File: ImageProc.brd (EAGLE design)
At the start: 49.8 x 23.2 mm, 119 parts, among them IC1 XC61GC3002HR-G, IC10 AT45DB642D-CNU, IC2 MIC5335-SPYMT, IC3 MIC5335-JGYMT, IC4 DSPIC33FJ128MC706A, IC5 AT86RF233-ZU, IC6 LTC6088, IC7 DRV8833RTY, IC8 DRV8833RTY, IC9 MPU-6000, P1 BAT+, P10 MD2, P11 EXT1, P12 EXT2, P13 EXT3, P14 EXT4, P16 EXT5, P2 BAT-, P3 MA1, P4 MA2, P5 MB1, P6 MB2, P7 MC1, P8 MC2, P9 MD1

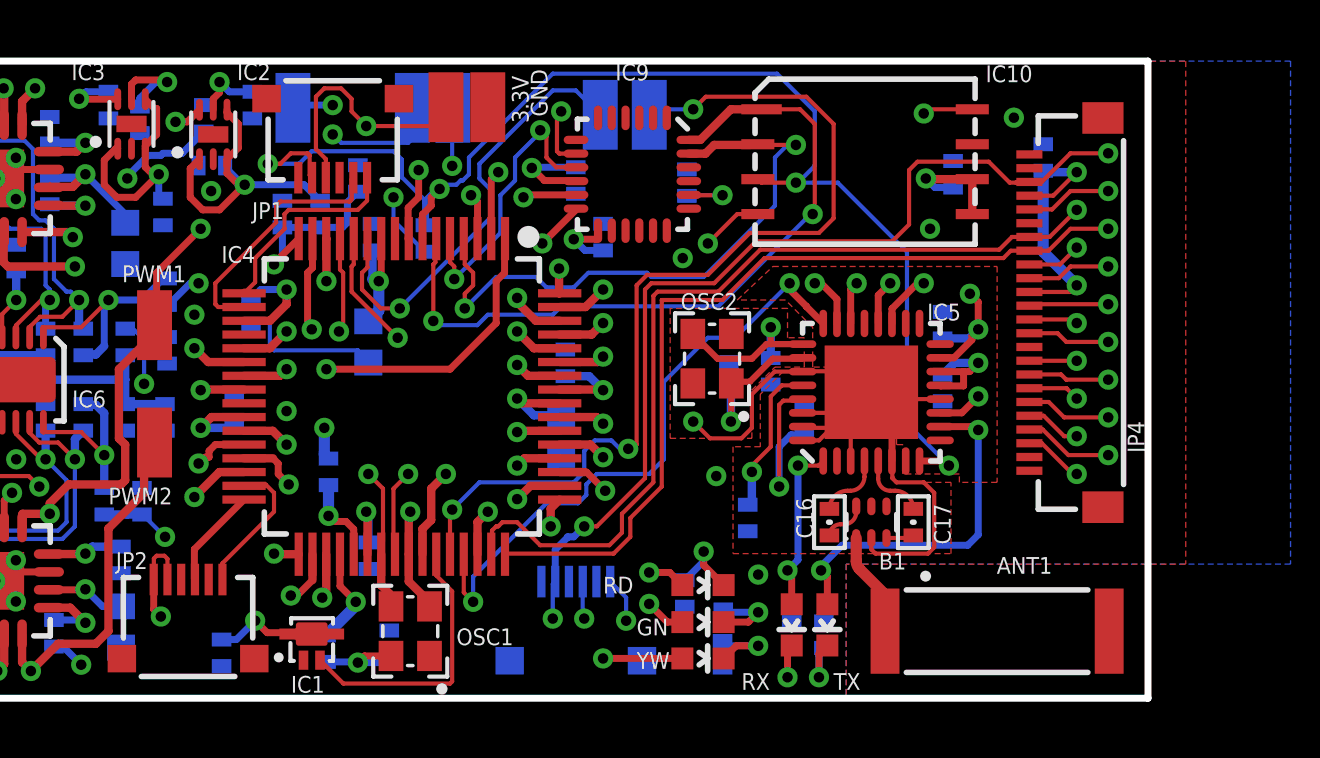
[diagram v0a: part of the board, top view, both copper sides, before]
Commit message: Initial strip of the IP2.5 Rev C board. dsPic and camera connector removed.
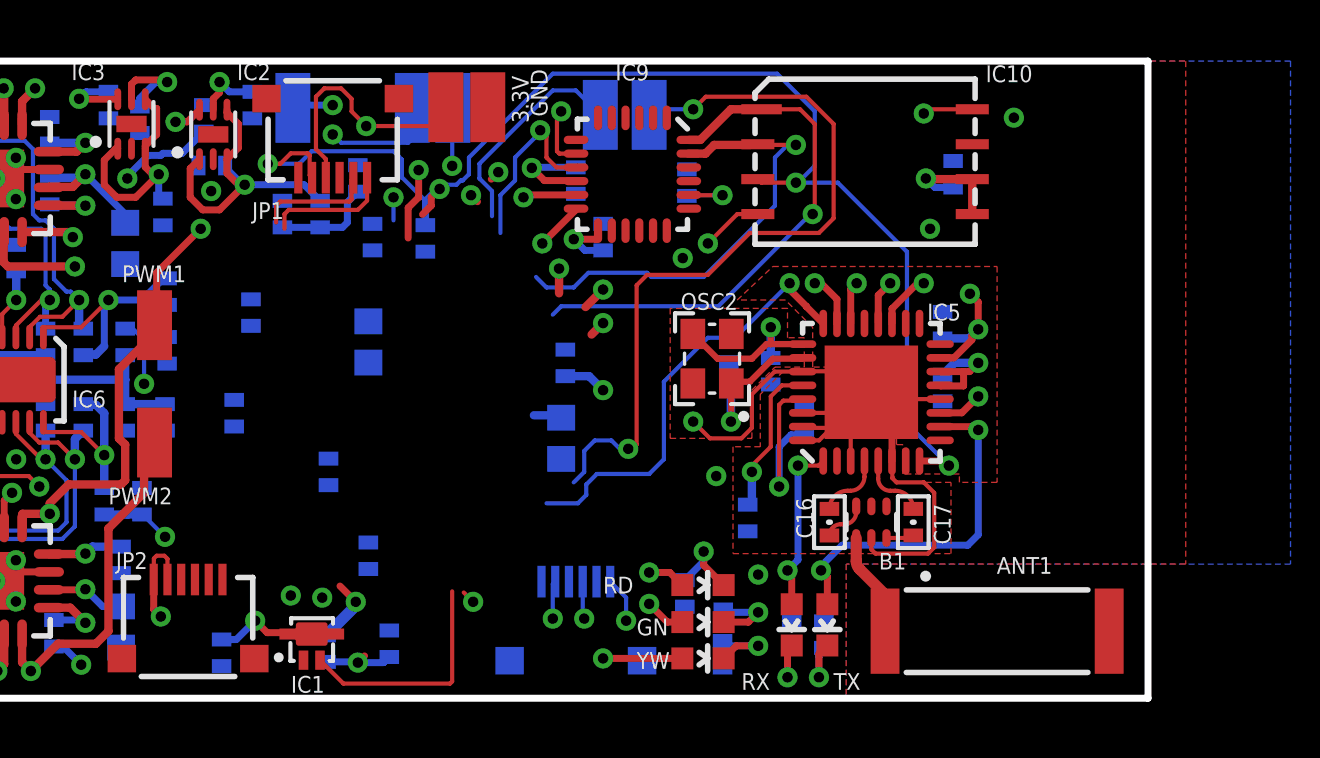
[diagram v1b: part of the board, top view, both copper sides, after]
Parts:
- removed C36: 0.1uF, biomimetic:0402-CAP
- removed IC4: DSPIC33FJ128MC706A, biomimetic:TQFP-64
- removed JP4: 51441-2493-C, biomimetic:MOLEX_52740-2490
- removed OSC1: ECS-2033-400, biomimetic:OSCILLATOR-SMD
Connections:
- removed net 40MHZ: IC4.39, JP4.12, OSC1.3
- removed net CAM_D0: IC4.46, JP4.6
- removed net CAM_D1: IC4.49, JP4.4
- removed net CAM_D2: IC4.50, JP4.3
- removed net CAM_D3: IC4.51, JP4.5
- removed net CAM_D4: IC4.52, JP4.7
- removed net CAM_D5: IC4.53, JP4.9
- removed net CAM_D6: IC4.54, JP4.11
- removed net CAM_D7: IC4.55, JP4.13
- removed net CAM_PCLK: IC4.59, JP4.8
- removed net CAM_PWDN: IC4.48, JP4.17
- removed net CAM_VSYNC: IC4.47, JP4.18
- net !RESET: no longer IC4.7
- net !SS1: no longer IC4.14
- net !SS2_1: no longer IC4.8
- net !SS2_2: no longer IC4.40
- net 1.8V: no longer JP4.15
- net 2.5V: no longer C36.2, JP4.14, JP4.21
- net 3.3V: no longer IC4.10, IC4.26, IC4.38, IC4.57, OSC1.4
- net AN1/RB1: no longer IC4.15
- net AN3/INDX/RB3: no longer IC4.13
- net AN4/QEA/IC7/RB4: no longer IC4.12
- net AN5/QEB/IC8/RB5: no longer IC4.11
- net BATT_LEVEL: no longer IC4.16
- net CAM_HREF: no longer IC4.58, JP4.16
- net GND: no longer C36.1, IC4.20, IC4.25, IC4.41, IC4.9, JP4.10, JP4.19, JP4.23, OSC1.2
- net GN_LED: no longer IC4.28
- net IC3/INT3/RD10: no longer IC4.44
- net IMU_IRQ: no longer IC4.42
- net LOWBATT_IRQ: no longer IC4.43
- net MOTOR_A_BEMF: no longer IC4.21
- net MOTOR_A_IN1: no longer IC4.61
- net MOTOR_A_IN2: no longer IC4.60
- net MOTOR_B_BEMF: no longer IC4.22
- net MOTOR_B_IN1: no longer IC4.63
- net MOTOR_B_IN2: no longer IC4.62
- net MOTOR_C_BEMF: no longer IC4.23
- net MOTOR_C_IN1: no longer IC4.1
- net MOTOR_C_IN2: no longer IC4.64
- net MOTOR_D_BEMF: no longer IC4.24
- net MOTOR_D_IN1: no longer IC4.3
- net MOTOR_D_IN2: no longer IC4.2
- net N$21: no longer IC4.19
- net N$28: no longer IC4.56
- net PGC: no longer IC4.17
- net PGD: no longer IC4.18
- net RADIO_IRQ: no longer IC4.45
- net RADIO_SLP_TR: no longer IC4.30
- net RD_LED: no longer IC4.27
- net SCK1: no longer IC4.35
- net SCK2: no longer IC4.4
- net SCL1: no longer IC4.37, JP4.20
- net SDA1: no longer IC4.36, JP4.22
- net SDI1: no longer IC4.34
- net SDI2: no longer IC4.5
- net SDO1: no longer IC4.33
- net SDO2: no longer IC4.6
- net U2RX: no longer IC4.31
- net U2TX: no longer IC4.32
- net YW_LED: no longer IC4.29
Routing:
- net SCL1: track 56.4 -> 1.37 mm, vias 3 -> 1
- net 2.5V: track 51.9 -> 2.59 mm, vias 3 -> 1
- net MOTOR_A_IN1: track 50.6 -> 1.92 mm
- net 1.8V: track 48.3 -> 3.48 mm, vias 2 -> 1
- net MOTOR_A_IN2: track 45.6 -> 1.77 mm, vias 3 -> 2
- net SDA1: track 45.6 -> 3.86 mm, vias 4 -> 2
- net RADIO_SLP_TR: track 41.3 -> 1.63 mm, vias 2 -> 1
- net 40MHZ: track 38.6 -> 0.00 mm, vias 2 -> 0
- net CAM_HREF: track 35.7 -> 1.95 mm, vias 3 -> 1
- net MOTOR_C_IN1: track 34.5 -> 1.37 mm, vias 2 -> 1
- net MOTOR_D_IN2: track 45.6 -> 12.9 mm
- net CAM_VSYNC: track 32.0 -> 0.00 mm, vias 1 -> 0
- net CAM_D0: track 31.9 -> 0.00 mm, vias 2 -> 0
- net MOTOR_D_IN1: track 33.2 -> 1.76 mm
- net CAM_D6: track 31.3 -> 0.00 mm, vias 2 -> 0
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- removed copper zone on layer 3, net 3.3V
- removed copper zone on layer 2, net GND
- removed copper zone on layer 3, net V_BATT
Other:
- board text added: "2014.08.06"
- board text added: "Andrew Pullin"
- board text added: "PSOCProc 1.0 Rev A"
- board text removed: "2013.04.01"
- board text removed: "BEARS!"
- board text removed: "Douglas Hutchings"
- board text removed: "GO"
- board text removed: "ImageProc 2.5 Rev. C"
- board text removed: "Ryan Julian"

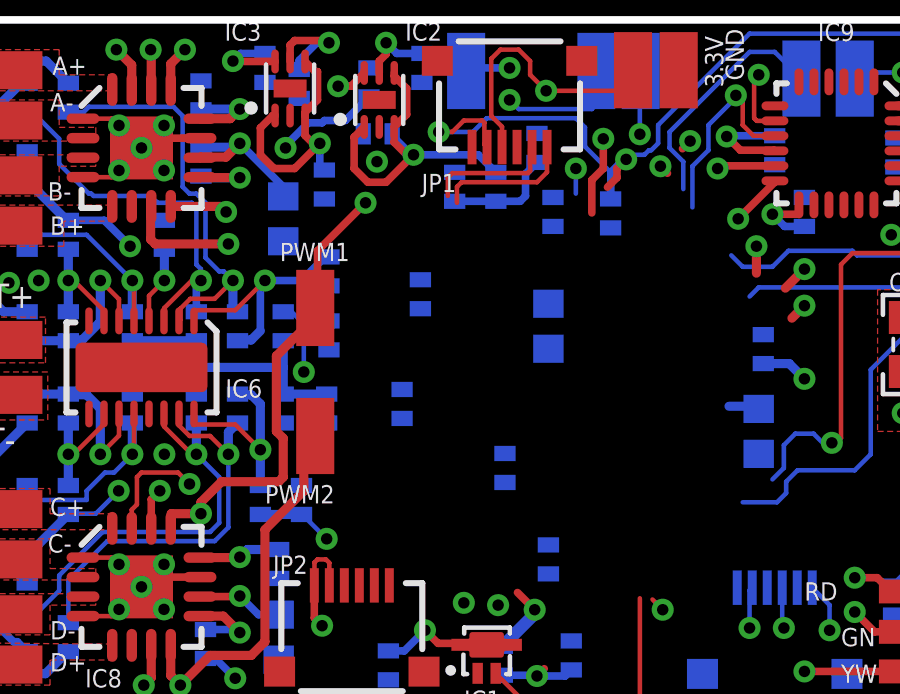
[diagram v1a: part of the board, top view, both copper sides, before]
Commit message: Initial placement of part with fixed functon pins in place, other pins as placeholders. Library part now active.
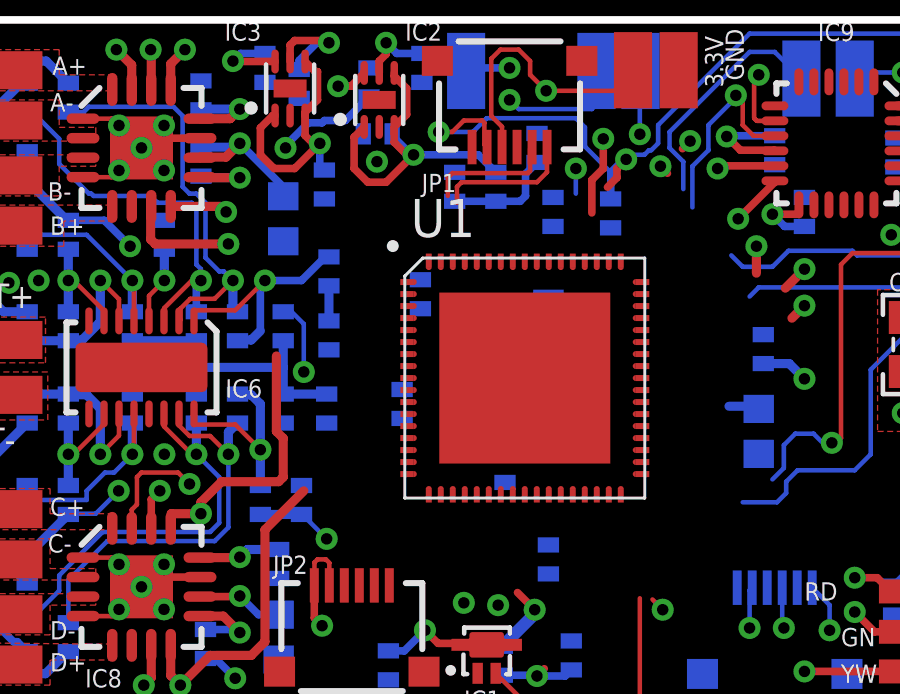
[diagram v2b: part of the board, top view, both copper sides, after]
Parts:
- removed PWM1, PWM2: EXT5, wirepad:SMD1,27-2,54
- added U1: CY8C5688LTI-LP086, pullin:68QFN
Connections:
- net MOTOR_C_IN2: no longer PWM1.1
- net MOTOR_D_IN2: no longer PWM2.1
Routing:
- net MOTOR_C_IN2: track 16.4 -> 9.99 mm, vias 3 -> 2
- net MOTOR_D_IN2: track 12.9 -> 10.9 mm
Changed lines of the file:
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@@
 <layers>
 <layer number="1" name="Top" color="4" fill="1" visible="yes" active="yes"/>
+<layer number="2" name="Route2" color="1" fill="3" visible="no" active="yes"/>
+<layer number="3" name="Route3" color="4" fill="3" visible="no" active="yes"/>
 <layer number="4" name="Route4" color="1" fill="4" visible="no" active="no"/>
 <layer number="5" name="Route5" color="4" fill="4" visible="no" active="no"/>
@@
 <layer number="18" name="Vias" color="2" fill="1" visible="yes" active="yes"/>
 <layer number="19" name="Unrouted" color="6" fill="1" visible="no" active="yes"/>
-<layer number="20" name="Dimension" color="15" fill="1" visible="no" active="yes"/>
-<layer number="21" name="tPlace" color="16" fill="1" visible="no" active="yes"/>
+<layer number="20" name="Dimension" color="15" fill="1" visible="yes" active="yes"/>
+<layer number="21" name="tPlace" color="16" fill="1" visible="yes" active="yes"/>
 <layer number="22" name="bPlace" color="14" fill="1" visible="no" active="yes"/>
-<layer number="23" name="tOrigins" color="15" fill="1" visible="no" active="yes"/>
+<layer number="23" name="tOrigins" color="15" fill="1" visible="yes" active="yes"/>
 <layer number="24" name="bOrigins" color="15" fill="1" visible="no" active="yes"/>
 <layer number="25" name="tNames" color="7" fill="1" visible="no" active="yes"/>
@@
 <layer number="54" name="bGND_GNDA" color="1" fill="9" visible="no" active="no"/>
 <layer number="56" name="wert" color="7" fill="1" visible="no" active="yes"/>
+<layer number="57" name="tCAD" color="12" fill="1" visible="no" active="no"/>
 <layer number="91" name="Nets" color="2" fill="1" visible="no" active="no"/>
 <layer number="92" name="Busses" color="1" fill="1" visible="no" active="no"/>
@@
 <layer number="97" name="Info" color="7" fill="1" visible="no" active="no"/>
 <layer number="98" name="Guide" color="14" fill="1" visible="no" active="no"/>
+<layer number="99" name="SpiceOrder" color="5" fill="1" visible="no" active="no"/>
 <layer number="100" name="Muster" color="7" fill="1" visible="no" active="no"/>
 <layer number="101" name="Patch_Top" color="12" fill="4" visible="no" active="yes"/>
@@
 <layer number="106" name="bPlate" color="7" fill="1" visible="no" active="yes"/>
 <layer number="107" name="Crop" color="7" fill="1" visible="no" active="yes"/>
+<layer number="108" name="tplace-old" color="10" fill="1" visible="no" active="yes"/>
+<layer number="109" name="ref-old" color="11" fill="1" visible="no" active="yes"/>
 <layer number="116" name="Patch_BOT" color="9" fill="4" visible="no" active="yes"/>
 <layer number="121" name="_tsilk" color="7" fill="1" visible="no" active="yes"/>
@@
 <layer number="144" name="Drill_legend" color="7" fill="1" visible="no" active="yes"/>
 <layer number="151" name="HeatSink" color="7" fill="1" visible="no" active="yes"/>
+<layer number="199" name="Contour" color="7" fill="1" visible="yes" active="yes"/>
 <layer number="200" name="200bmp" color="1" fill="10" visible="no" active="yes"/>
 <layer number="201" name="201bmp" color="2" fill="10" visible="no" active="yes"/>
@@
 <element name="IC2" library="biomimetic" package="MLF-6" value="MIC5335-SPYMT" x="15.8496" y="20.4978" smashed="yes">
 <attribute name="NAME" x="16.7132" y="22.4726" size="0.6096" layer="25" font="vector" ratio="25"/>
+<attribute name="DIGIKEY" value="576-1949-1-ND" x="15.8496" y="20.4978" size="1.778" layer="27" display="off"/>
 </element>
 <element name="IC3" library="biomimetic" package="MLF-6" value="MIC5335-JGYMT" x="12.8778" y="20.8788" smashed="yes">
 <attribute name="NAME" x="10.6934" y="22.4726" size="0.6096" layer="25" font="vector" ratio="25"/>
+<attribute name="DIGIKEY" value="576-3589-1-ND" x="12.8778" y="20.8788" size="1.778" layer="27" display="off"/>
 </element>
 <element name="C35" library="biomimetic" package="0402-CAP" value="2.2uF" x="12.4968" y="5.0292" locked="yes" smashed="yes" rot="MR270">
@@
 <element name="JP1" library="biomimetic" package="MOLEX_503480-0600" value="MOLEX_503480-0600" x="20.193" y="20.6502" smashed="yes" rot="R180">
 <attribute name="NAME" x="18.415" y="18.034" size="0.6096" layer="25" font="vector" ratio="25" rot="R180"/>
+<attribute name="DIGIKEY" value="WM1387CT-ND" x="20.193" y="20.6502" size="1.778" layer="27" rot="R180" display="off"/>
 </element>
 <element name="JP2" library="biomimetic" package="MOLEX_503480-0600" value="MOLEX_503480-0600" x="14.9352" y="2.5908" locked="yes" smashed="yes">
 <attribute name="NAME" x="13.462" y="5.3086" size="0.6096" layer="25" font="vector" ratio="25" rot="R180"/>
+<attribute name="DIGIKEY" value="WM1387CT-ND" x="14.9352" y="2.5908" size="1.778" layer="27" display="off"/>
 </element>
 <element name="JP3" library="biomimetic" package="MOLEX_503480-0600" value="MOLEX_503480-0600" x="29.0322" y="2.5146" smashed="yes" rot="MR0">
 <attribute name="NAME" x="30.3022" y="5.0546" size="0.6096" layer="26" font="vector" ratio="25" rot="MR0"/>
+<attribute name="DIGIKEY" value="WM1387CT-ND" x="29.0322" y="2.5146" size="1.778" layer="28" rot="MR0" display="off"/>
 </element>
 <element name="B1" library="biomimetic" package="0603-BALUN" value="HHM1710D1" x="39.7764" y="6.4008" locked="yes" smashed="yes">
@@
 <attribute name="NAME" x="27.3178" y="20.9172" size="0.6096" layer="25" font="vector" ratio="25" rot="R90"/>
 </element>
-<element name="PWM1" library="wirepad" package="SMD1,27-2,54" value="EXT5" x="13.716" y="13.5636" smashed="yes" rot="R180">
-<attribute name="DESIGN_NAME" value="ImageProc 2.5" x="13.716" y="13.5636" size="1.778" layer="27" rot="R180" display="off"/>
-<attribute name="AUTHOR" value="Ryan Julian (ryanjulian@berkeley.edu)" x="13.716" y="13.5636" size="1.778" layer="27" rot="R180" display="off"/>
-<attribute name="REVISION" value="B" x="13.716" y="13.5636" size="1.778" layer="27" rot="R180" display="off"/>
-<attribute name="YEAR" value="2012" x="13.716" y="13.5636" size="1.778" layer="27" rot="R180" display="off"/>
-<attribute name="NAME" x="12.5352" y="15.1256" size="0.6096" layer="25" font="vector" ratio="25"/>
-<attribute name="PWM1" value="MOTOR_C_IN_2" x="13.716" y="13.5636" size="1.778" layer="27" rot="R180" display="off"/>
-</element>
-<element name="PWM2" library="wirepad" package="SMD1,27-2,54" value="EXT5" x="13.716" y="9.2964" smashed="yes" rot="R180">
-<attribute name="DESIGN_NAME" value="ImageProc 2.5" x="13.716" y="9.2964" size="1.778" layer="27" rot="R180" display="off"/>
-<attribute name="AUTHOR" value="Ryan Julian (ryanjulian@berkeley.edu)" x="13.716" y="9.2964" size="1.778" layer="27" rot="R180" display="off"/>
-<attribute name="REVISION" value="B" x="13.716" y="9.2964" size="1.778" layer="27" rot="R180" display="off"/>
-<attribute name="YEAR" value="2012" x="13.716" y="9.2964" size="1.778" layer="27" rot="R180" display="off"/>
-<attribute name="NAME" x="14.3634" y="7.6582" size="0.6096" layer="25" font="vector" ratio="25" rot="R180"/>
-<attribute name="PWM2" value="MOTOR_D_IN_2" x="13.716" y="9.2964" size="1.778" layer="27" rot="R180" display="off"/>
-</element>
+<element name="U1" library="pullin" package="68QFN" value="CY8C5688LTI-LP086" x="20.701" y="11.2268"/>
 </elements>
 <signals>
@@
 <via x="28.4226" y="15.621" extent="1-16" drill="0.381"/>
 <wire x1="28.4226" y1="14.7228" x2="28.4226" y2="15.621" width="0.3048" layer="1"/>
-<via x="15.3924" y="17.0688" extent="1-16" drill="0.381"/>
-<wire x1="15.3924" y1="17.0688" x2="13.7922" y2="15.4686" width="0.254" layer="1"/>
-<contactref element="PWM1" pad="1"/>
+<wire x1="15.3924" y1="17.0688" x2="15.3924" y2="17.0688" width="0" layer="19" extent="1-16"/>
+<wire x1="15.3924" y1="17.0688" x2="13.7922" y2="15.4686" width="0" layer="19" extent="1-16"/>
 <wire x1="9.906" y1="6.7056" x2="9.906" y2="7.0866" width="0.3048" layer="1"/>
 <wire x1="9.906" y1="7.0866" x2="10.5918" y2="7.7724" width="0.3048" layer="1"/>
 <wire x1="10.5918" y1="7.7724" x2="12.4968" y2="7.7724" width="0.3048" layer="1"/>
-<wire x1="13.7922" y1="15.4686" x2="13.7922" y2="13.6398" width="0.254" layer="1"/>
-<wire x1="13.7922" y1="13.6398" x2="13.716" y2="13.5636" width="0.254" layer="1"/>
-<wire x1="13.7922" y1="13.6398" x2="13.7922" y2="13.335" width="0.3048" layer="1"/>
-<wire x1="13.7922" y1="13.335" x2="12.4206" y2="11.9634" width="0.3048" layer="1"/>
+<wire x1="13.7922" y1="15.4686" x2="13.7922" y2="13.6398" width="0" layer="19" extent="1-16"/>
+<wire x1="13.7922" y1="13.6398" x2="13.7922" y2="13.335" width="0" layer="19" extent="1-16"/>
+<wire x1="13.7922" y1="13.335" x2="12.4206" y2="11.9634" width="0" layer="19" extent="1-16"/>
 <wire x1="12.4206" y1="11.9634" x2="12.4206" y2="9.4488" width="0.3048" layer="1"/>
 <wire x1="12.4206" y1="9.4488" x2="12.6492" y2="9.2202" width="0.3048" layer="1"/>
@@
 <wire x1="26.289" y1="19.2024" x2="26.2128" y2="19.1262" width="0.3048" layer="1"/>
 <wire x1="26.2128" y1="19.1262" x2="25.9576" y2="18.871" width="0.254" layer="1"/>
-<contactref element="PWM2" pad="1"/>
 <wire x1="12.0396" y1="2.4384" x2="11.5824" y2="1.9812" width="0.3048" layer="1"/>
 <wire x1="11.5824" y1="1.9812" x2="10.2108" y2="1.9812" width="0.3048" layer="1"/>
@@
 <wire x1="12.0396" y1="2.4384" x2="12.0396" y2="6.1722" width="0.3048" layer="1"/>
 <wire x1="12.0396" y1="6.1722" x2="13.335" y2="7.4676" width="0.3048" layer="1"/>
-<wire x1="13.335" y1="7.4676" x2="13.335" y2="8.9154" width="0.3048" layer="1"/>
-<wire x1="13.335" y1="8.9154" x2="13.716" y2="9.2964" width="0.3048" layer="1"/>
-<wire x1="13.716" y1="9.2964" x2="25.9576" y2="18.871" width="0" layer="19" extent="1-1"/>
+<wire x1="13.335" y1="7.4676" x2="13.335" y2="8.9154" width="0" layer="19" extent="1-16"/>
+<wire x1="13.335" y1="8.9154" x2="25.9576" y2="18.871" width="0" layer="19" extent="1-1"/>
 </signal>
 <signal name="MOTOR_A_OUT2">
